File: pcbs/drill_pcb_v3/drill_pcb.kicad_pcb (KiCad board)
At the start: 2 copper layers, 105 x 103 mm, 49 parts, among them J1 24V IN, J10 LIMIT SWITCH BOTTOM, J11 DEEP WEIGHT SENSOR, J12 SURFACE WEIGHT SENSOR, J13 SERVO 1, J14 SERVO 2, J15 STEPPER STORAGE, J16 TEST PADS, J2 uC COMMUNICATION, J3 ENCODER VERTICAL DRIVE, J4 LIMIT SWITCH TOP, J5 HEIGHT SENSOR, J6 STEPPER VERTICAL DRIVE, J7 DC MOTOR 24 V, J8 DC MOTOR UART, J9 ENCODER STORAGE, Q3 SI2333-TP, U1 ESP32-DevKitC, U2 LM3940, U3 INA219BxD

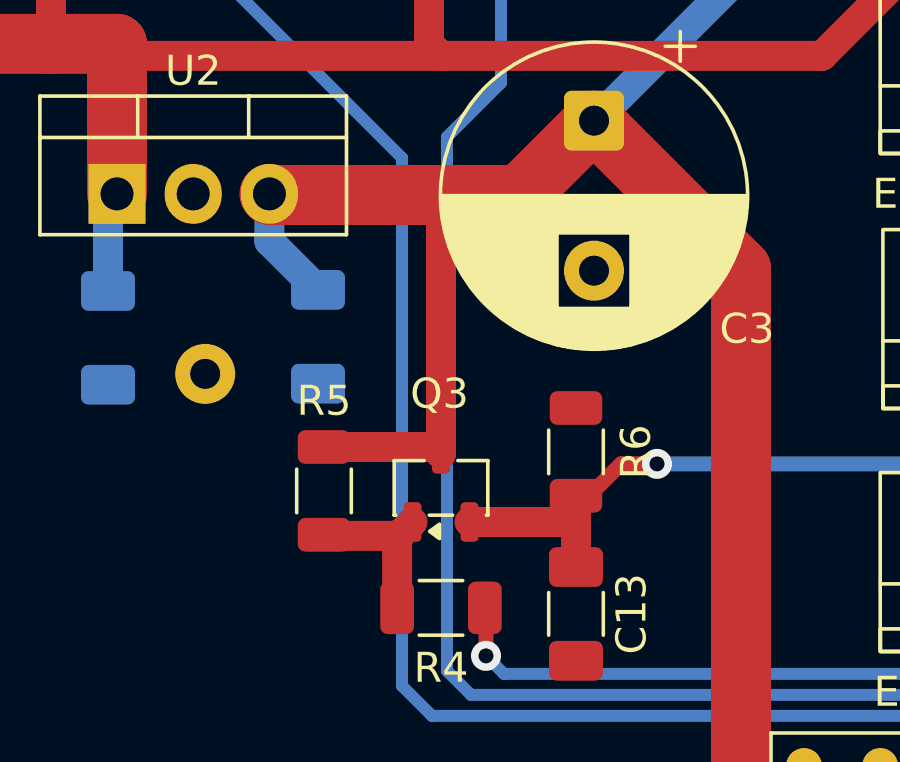
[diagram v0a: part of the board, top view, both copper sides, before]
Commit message: Resolved mosfet misplacement for board v3. Deleted history.
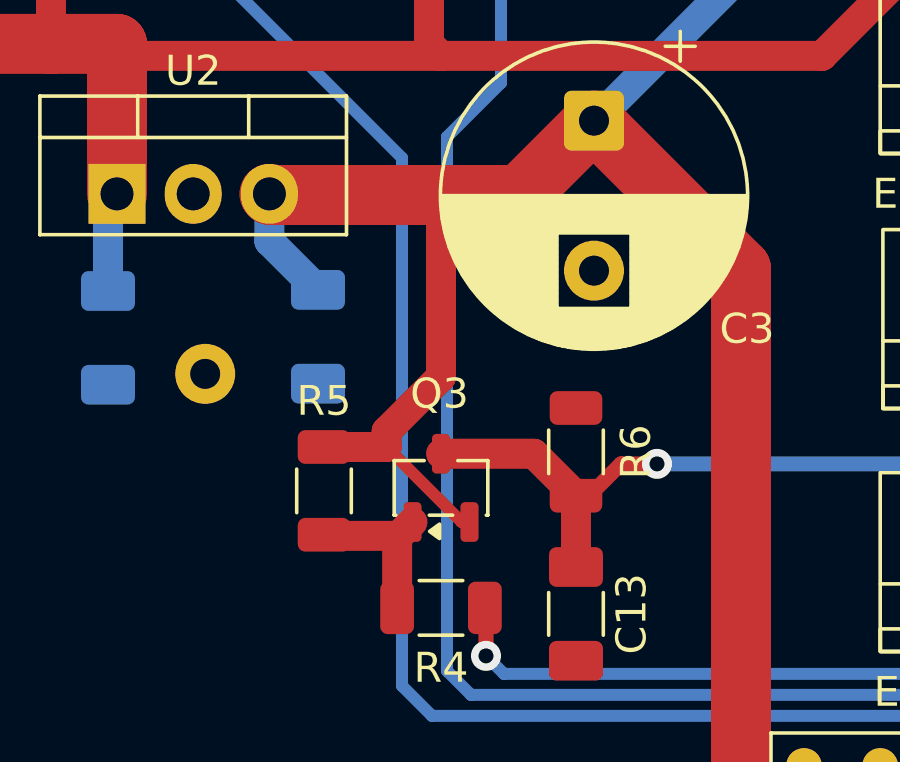
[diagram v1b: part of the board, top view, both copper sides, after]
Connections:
- Q3 pad 2: +3.3VP -> +3.3V
- Q3 pad 3: +3.3V -> +3.3VP
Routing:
- net +3.3V: track 256.6 -> 259.0 mm
- net +3.3VP: track 141.2 -> 142.7 mm
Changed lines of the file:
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@@
 		(capping no)
 		(filling no)
-		(zone_defaults)
 		(pcbplotparams
 			(layerselection 0x00000000_00000000_55555555_5755f5ff)
@@
 			(layers "F.Cu" "F.Mask" "F.Paste")
 			(roundrect_rratio 0.25)
-			(net "+3.3VP")
+			(net "+3.3V")
 			(pinfunction "S_2")
 			(pintype "passive")
@@
 			(layers "F.Cu" "F.Mask" "F.Paste")
 			(roundrect_rratio 0.25)
-			(net "+3.3V")
+			(net "+3.3VP")
 			(pinfunction "D_3")
 			(pintype "passive")
@@
 	)
 	(segment
+		(start 59.689106 66.4375)
+		(end 57.6 66.4375)
+		(width 1)
+		(layer "F.Cu")
+		(net "+3.3V")
+	)
+	(segment
 		(start 71.5 88.01)
 		(end 73.66 90.17)
@@
 	)
 	(segment
-		(start 73.025 49.225)
-		(end 73.95 48.3)
+		(start 59.689106 65.910894)
+		(end 59.689106 66.4375)
 		(width 1)
 		(layer "F.Cu")
@@
 	)
 	(segment
-		(start 55.78 58)
-		(end 55.8175 58.0375)
-		(width 2)
+		(start 62.189106 68.9375)
+		(end 62.45 68.9375)
+		(width 0.4)
+		(layer "F.Cu")
+		(net "+3.3V")
+	)
+	(segment
+		(start 73.025 49.225)
+		(end 73.95 48.3)
+		(width 1)
 		(layer "F.Cu")
 		(net "+3.3V")
@@
 	(segment
 		(start 61.5 58.1375)
-		(end 61.4 58.0375)
+		(end 61.5 64.1)
 		(width 1)
 		(layer "F.Cu")
@@
 	)
 	(segment
+		(start 55.78 58)
+		(end 55.8175 58.0375)
+		(width 2)
+		(layer "F.Cu")
+		(net "+3.3V")
+	)
+	(segment
 		(start 71.5 60.5)
 		(end 71.5 88.01)
@@
 	)
 	(segment
-		(start 117.3 60.2)
-		(end 117.3 59.2)
-		(width 1)
+		(start 59.689106 66.4375)
+		(end 62.189106 68.9375)
+		(width 0.4)
 		(layer "F.Cu")
 		(net "+3.3V")
 	)
 	(segment
-		(start 57.6 66.4375)
-		(end 59 66.4375)
+		(start 117.3 60.2)
+		(end 117.3 59.2)
 		(width 1)
 		(layer "F.Cu")
@@
 	)
 	(segment
-		(start 61.5 66.6625)
+		(start 61.4 58.0375)
 		(end 61.5 58.1375)
 		(width 1)
@@
 	)
 	(segment
-		(start 61.5 66.6625)
-		(end 61.275 66.4375)
-		(width 1)
-		(layer "F.Cu")
-		(net "+3.3V")
-	)
-	(segment
 		(start 73.66 90.17)
 		(end 73.66 100.33)
@@
 	)
 	(segment
-		(start 100.6 69)
-		(end 100.6 60.9)
+		(start 61.5 64.1)
+		(end 59.689106 65.910894)
 		(width 1)
 		(layer "F.Cu")
@@
 	)
 	(segment
-		(start 61.275 66.4375)
-		(end 59 66.4375)
+		(start 100.6 69)
+		(end 100.6 60.9)
 		(width 1)
 		(layer "F.Cu")
@@
 	)
 	(segment
-		(start 66.4375 68.0625)
-		(end 66 68.0625)
-		(width 0.5)
-		(layer "F.Cu")
-		(net "+3.3VP")
-	)
-	(segment
-		(start 68.7 67)
-		(end 67.5 67)
-		(width 0.5)
+		(start 66 68.0625)
+		(end 64.6 66.6625)
+		(width 1)
 		(layer "F.Cu")
 		(net "+3.3VP")
 	)
 	(segment
-		(start 62.45 68.9375)
-		(end 65.9 68.9375)
+		(start 66 68.0625)
+		(end 66 70.4375)
 		(width 1)
 		(layer "F.Cu")
@@
 	)
 	(segment
-		(start 65.9 68.9375)
-		(end 66 69.0375)
-		(width 1)
+		(start 66.4375 68.0625)
+		(end 66 68.0625)
+		(width 0.5)
 		(layer "F.Cu")
 		(net "+3.3VP")
 	)
 	(segment
-		(start 66 68.0625)
-		(end 66 69.0375)
-		(width 1)
+		(start 68.7 67)
+		(end 67.5 67)
+		(width 0.5)
 		(layer "F.Cu")
 		(net "+3.3VP")
@@
 	)
 	(segment
-		(start 66 69.0375)
-		(end 66 70.4375)
+		(start 64.6 66.6625)
+		(end 61.5 66.6625)
 		(width 1)
 		(layer "F.Cu")

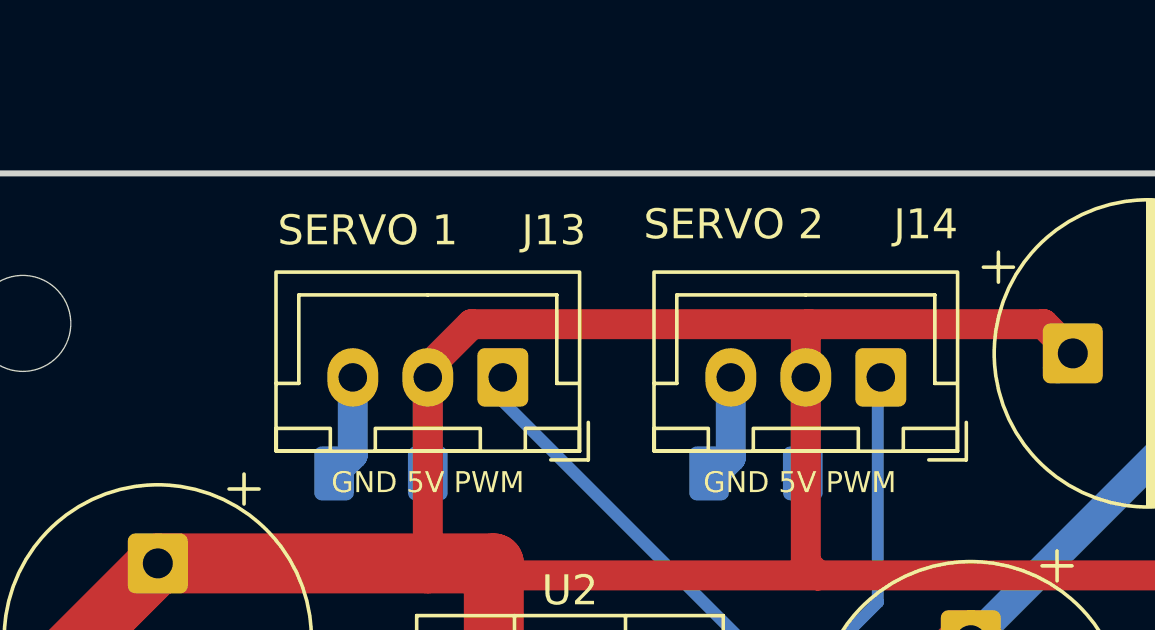
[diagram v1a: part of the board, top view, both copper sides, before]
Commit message: ADC reset and Servo labels updated
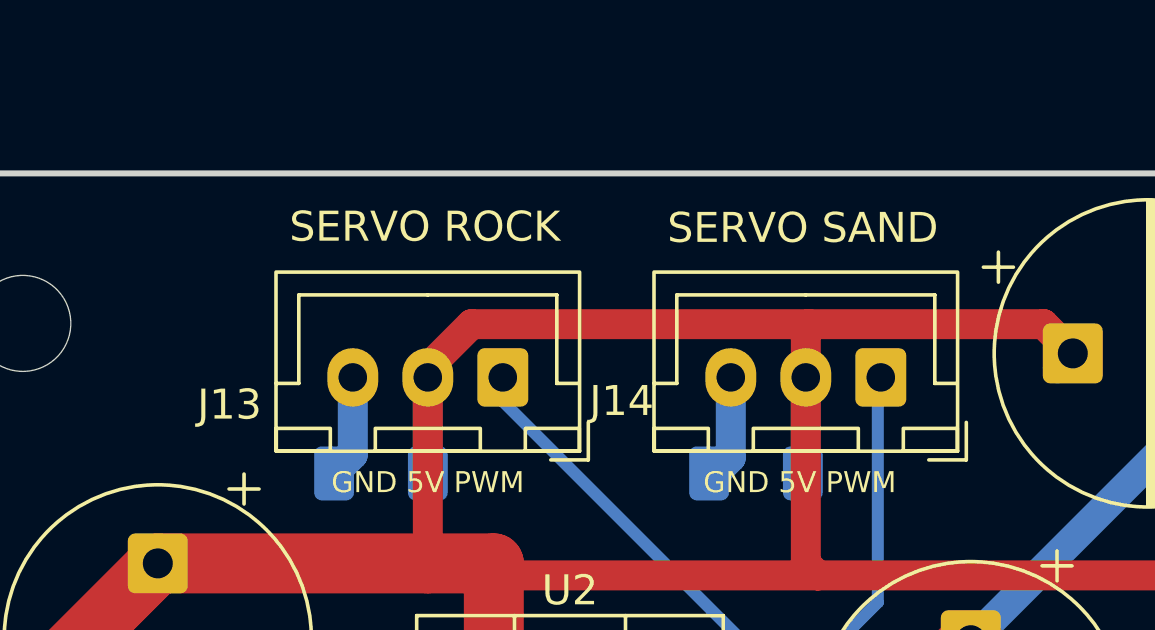
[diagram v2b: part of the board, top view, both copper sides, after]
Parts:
- J13: value SERVO 1 -> SERVO ROCK
- J14: value SERVO 2 -> SERVO SAND
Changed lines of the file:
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@@
 		(tags "connector JST XH vertical")
 		(property "Reference" "J13"
-			(at -1.7 4.9 0)
+			(at 9.11 -0.91 0)
 			(layer "F.SilkS")
 			(effects
@@
 			)
 		)
-		(property "Value" "SERVO 1"
-			(at 4.5 4.9 0)
+		(property "Value" "SERVO ROCK"
+			(at 2.6 5.02 0)
 			(layer "F.SilkS")
 			(effects
@@
 		(tags "connector JST XH vertical")
 		(property "Reference" "J14"
-			(at -1.5 5.1 0)
+			(at 8.64 -0.79 0)
 			(layer "F.SilkS")
 			(effects
@@
 			)
 		)
-		(property "Value" "SERVO 2"
-			(at 4.9 5.1 0)
+		(property "Value" "SERVO SAND"
+			(at 2.6 4.98 0)
 			(layer "F.SilkS")
 			(effects
